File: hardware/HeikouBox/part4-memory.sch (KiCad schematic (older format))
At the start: 10 parts, among them U401 K4S281632-UC60

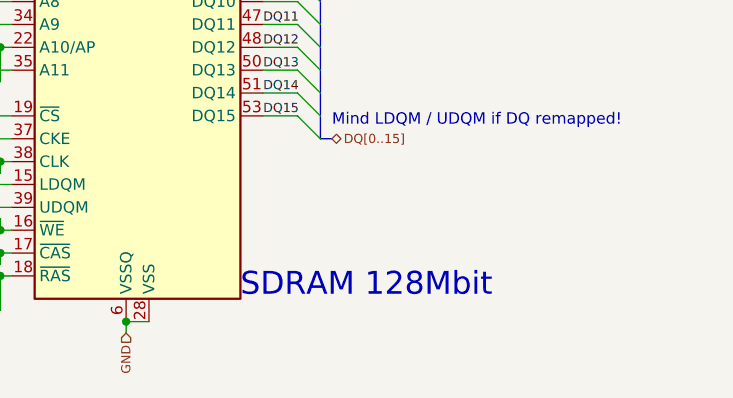
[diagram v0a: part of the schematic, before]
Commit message: Replace MCU with blue pill, tidy up
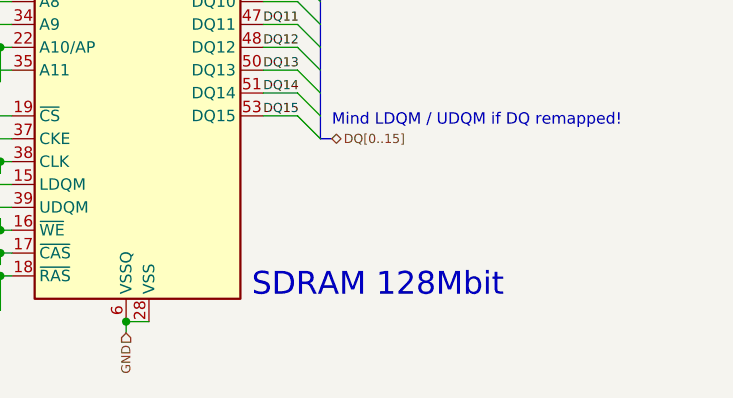
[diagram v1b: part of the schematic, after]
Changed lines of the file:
@@
 $Descr A4 11693 8268
 encoding utf-8
-Sheet 6 7
+Sheet 5 6
 Title "HeikouBox Mainboard - Memory"
 Date "2021-03-17"
@@
 	1    0    0    -1
 $EndComp
-Text Notes 2400 3250 0    100  ~ 0
+Text Notes 2450 3250 0    100  ~ 0
 SDRAM 128Mbit
 Connection ~ 1900 3350

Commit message: Mostly routed board
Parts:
- added C405: 100n, Capacitor_SMD:C_0603_1608Metric_Pad1.08x0.95mm_HandSolder, symbol Device:C
- C401, C402, C403, C404: footprint Capacitor_SMD:C_0603_1608Metric_Pad1.05x0.95mm_HandSolder -> Capacitor_SMD:C_0603_1608Metric_Pad1.08x0.95mm_HandSolder
- R401, R402, R403, R404, R405: footprint Resistor_SMD:R_0603_1608Metric_Pad1.05x0.95mm_HandSolder -> Resistor_SMD:R_0603_1608Metric_Pad0.98x0.95mm_HandSolder
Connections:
- net 3V3: now also C405.1
- net GND: now also C405.2
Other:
- moved on the sheet: C401, C402, C403, C404

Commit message: Mainboard v0.1 PCB ready for export
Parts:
- removed R401, R402, R403, R404, R405: 1K, Resistor_SMD:R_0603_1608Metric_Pad0.98x0.95mm_HandSolder, symbol Device:R
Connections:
- net CKE is gone; now on net 3V3: U401.37 (CKE)
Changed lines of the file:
@@
 $Descr A4 11693 8268
 encoding utf-8
-Sheet 5 6
+Sheet 4 6
 Title "HeikouBox Mainboard - Memory"
 Date "2021-03-17"
@@
 Wire Wire Line
 	1200 1050 1400 1050
-Wire Wire Line
-	1300 3150 1350 3150
-Wire Wire Line
-	1300 3050 1350 3050
 Wire Wire Line
 	1900 3350 2000 3350
@@
 	1900 750  2000 750
 Connection ~ 1900 750
-Wire Wire Line
-	1300 2650 1350 2650
-Wire Wire Line
-	1300 2950 1350 2950
 Text Notes 3900 2500 0    50   ~ 0
 Mind LDQM / UDQM if DQ remapped!
@@
 Text HLabel 1300 3150 0    40   Input ~ 0
 RAS
-Text HLabel 1300 2550 0    40   Input ~ 0
-CKE
 Text Label 1200 1150 0    40   ~ 0
 A0
@@
 Wire Wire Line
 	5650 1050 6050 1050
-Text HLabel 750  3100 0    40   Input ~ 0
-XCAS
-Text HLabel 750  2900 0    40   Input ~ 0
-XWE
-Wire Wire Line
-	1350 2650 1350 2700
-Connection ~ 1350 2650
-Wire Wire Line
-	1350 2650 1400 2650
-Wire Wire Line
-	1350 2900 1350 2950
-Connection ~ 1350 2950
-Wire Wire Line
-	1350 2950 1400 2950
-Wire Wire Line
-	1350 3100 1350 3050
-Connection ~ 1350 3050
-Wire Wire Line
-	1350 3050 1400 3050
-Wire Wire Line
-	1200 2150 1350 2150
-Wire Wire Line
-	1350 2150 1350 2300
-Connection ~ 1350 2150
-Wire Wire Line
-	1350 2150 1400 2150
-Text HLabel 750  2300 0    40   Input ~ 0
-XAP
-Wire Wire Line
-	750  2300 800  2300
-Wire Wire Line
-	1100 2700 1350 2700
-Wire Wire Line
-	1350 2300 1100 2300
 Text HLabel 1300 2450 0    40   Input ~ 0
 GND
 Wire Wire Line
-	1100 2900 1350 2900
-Wire Wire Line
-	750  2900 800  2900
-Wire Wire Line
-	1100 3100 1350 3100
-Wire Wire Line
-	750  3100 800  3100
-Wire Wire Line
 	1300 2450 1400 2450
-Wire Wire Line
-	750  2700 800  2700
-Text HLabel 750  2700 0    40   Input ~ 0
-XCLK
-Text HLabel 750  3300 0    40   Input ~ 0
-XRAS
-Wire Wire Line
-	1100 3300 1350 3300
-Wire Wire Line
-	750  3300 800  3300
-Wire Wire Line
-	1350 3300 1350 3150
-Connection ~ 1350 3150
-Wire Wire Line
-	1350 3150 1400 3150
-Wire Wire Line
-	1300 2550 1400 2550
-$Comp
-L Device:R R?
-U 1 1 683F9E5B
-P 950 3100
-AR Path="/683F9E5B" Ref="R?"  Part="1"
-AR Path="/646E3FCF/683F9E5B" Ref="R?"  Part="1"
-AR Path="/729F40C7/683F9E5B" Ref="R403"  Part="1"
-F 0 "R403" V 850 3100 50  0000 C CNN
-F 1 "1K" V 950 3100 50  0000 C CNN
-F 2 "Resistor_SMD:R_0603_1608Metric_Pad0.98x0.95mm_HandSolder" V 880 3100 50  0001 C CNN
-F 3 "~" H 950 3100 50  0001 C CNN
-	1    950  3100
-	0    1    1    0
-$EndComp
-$Comp
-L Device:R R?
-U 1 1 686DF49A
-P 950 3300
-AR Path="/686DF49A" Ref="R?"  Part="1"
-AR Path="/646E3FCF/686DF49A" Ref="R?"  Part="1"
-AR Path="/729F40C7/686DF49A" Ref="R404"  Part="1"
-F 0 "R404" V 850 3300 50  0000 C CNN
-F 1 "1K" V 950 3300 50  0000 C CNN
-F 2 "Resistor_SMD:R_0603_1608Metric_Pad0.98x0.95mm_HandSolder" V 880 3300 50  0001 C CNN
-F 3 "~" H 950 3300 50  0001 C CNN
-	1    950  3300
-	0    1    1    0
-$EndComp
-$Comp
-L Device:R R?
-U 1 1 683FD000
-P 950 2900
-AR Path="/683FD000" Ref="R?"  Part="1"
-AR Path="/646E3FCF/683FD000" Ref="R?"  Part="1"
-AR Path="/729F40C7/683FD000" Ref="R402"  Part="1"
-F 0 "R402" V 850 2900 50  0000 C CNN
-F 1 "1K" V 950 2900 50  0000 C CNN
-F 2 "Resistor_SMD:R_0603_1608Metric_Pad0.98x0.95mm_HandSolder" V 880 2900 50  0001 C CNN
-F 3 "~" H 950 2900 50  0001 C CNN
-	1    950  2900
-	0    1    1    0
-$EndComp
-$Comp
-L Device:R R?
-U 1 1 683DF4DC
-P 950 2700
-AR Path="/683DF4DC" Ref="R?"  Part="1"
-AR Path="/646E3FCF/683DF4DC" Ref="R?"  Part="1"
-AR Path="/729F40C7/683DF4DC" Ref="R401"  Part="1"
-F 0 "R401" V 850 2700 50  0000 C CNN
-F 1 "1K" V 950 2700 50  0000 C CNN
-F 2 "Resistor_SMD:R_0603_1608Metric_Pad0.98x0.95mm_HandSolder" V 880 2700 50  0001 C CNN
-F 3 "~" H 950 2700 50  0001 C CNN
-	1    950  2700
-	0    1    1    0
-$EndComp
-$Comp
-L Device:R R?
-U 1 1 6848DBCA
-P 950 2300
-AR Path="/6848DBCA" Ref="R?"  Part="1"
-AR Path="/646E3FCF/6848DBCA" Ref="R?"  Part="1"
-AR Path="/729F40C7/6848DBCA" Ref="R405"  Part="1"
-F 0 "R405" V 850 2300 50  0000 C CNN
-F 1 "1K" V 950 2300 50  0000 C CNN
-F 2 "Resistor_SMD:R_0603_1608Metric_Pad0.98x0.95mm_HandSolder" V 880 2300 50  0001 C CNN
-F 3 "~" H 950 2300 50  0001 C CNN
-	1    950  2300
-	0    1    1    0
-$EndComp
 Text Notes 4950 700  0    50   ~ 0
 Place near SDRAM
@@
 Wire Wire Line
 	6450 1050 6050 1050
+Wire Wire Line
+	1200 2150 1400 2150
+Wire Wire Line
+	1300 2650 1400 2650
+Wire Wire Line
+	1300 2950 1400 2950
+Wire Wire Line
+	1300 3050 1400 3050
+Wire Wire Line
+	1300 3150 1400 3150
+Text HLabel 1300 2550 0    40   Input ~ 0
+3V3
+Wire Wire Line
+	1300 2550 1400 2550
 Wire Bus Line
 	1100 1050 1100 2150

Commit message: Tidy up power nets
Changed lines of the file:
@@
 Connection ~ 1900 3350
 Wire Wire Line
-	1900 3400 1900 3350
-Text HLabel 1900 3400 3    40   Input ~ 0
-GND
-Wire Wire Line
-	1900 700  1900 750
-Text HLabel 1900 700  1    40   Input ~ 0
-3V3
-Wire Wire Line
-	4850 700  4850 750
-Text HLabel 4850 700  1    40   Input ~ 0
-3V3
+	1900 3450 1900 3350
+Wire Wire Line
+	1900 650  1900 750
+Text HLabel 700  3850 0    40   Input ~ 0
+3V3
+Wire Wire Line
+	4850 650  4850 750
 Connection ~ 4850 750
 Wire Wire Line
-	4850 1100 4850 1050
-Text HLabel 4850 1100 3    40   Input ~ 0
-GND
+	4850 1150 4850 1050
 Connection ~ 4850 1050
 Wire Bus Line
@@
 Wire Wire Line
 	5650 1050 6050 1050
-Text HLabel 1300 2450 0    40   Input ~ 0
-GND
 Wire Wire Line
 	1300 2450 1400 2450
@@
 Wire Wire Line
 	1300 3150 1400 3150
-Text HLabel 1300 2550 0    40   Input ~ 0
-3V3
 Wire Wire Line
 	1300 2550 1400 2550
+Text Label 800  3850 0    40   ~ 8
+3V3
+Wire Wire Line
+	800  3850 700  3850
+Text Label 1900 650  1    40   ~ 8
+3V3
+Text HLabel 700  3950 0    40   Input ~ 0
+GND
+Text Label 800  3950 0    40   ~ 8
+GND
+Wire Wire Line
+	800  3950 700  3950
+Text Label 1900 3450 3    40   ~ 8
+GND
+Text Label 1300 2450 2    40   ~ 8
+GND
+Text Label 1300 2550 2    40   ~ 8
+3V3
+Text Label 4850 650  1    40   ~ 8
+3V3
+Text Label 4850 1150 3    40   ~ 8
+GND
 Wire Bus Line
 	1100 1050 1100 2150
